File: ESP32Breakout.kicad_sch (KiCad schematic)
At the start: 7 parts, among them U1 ESP32-S3

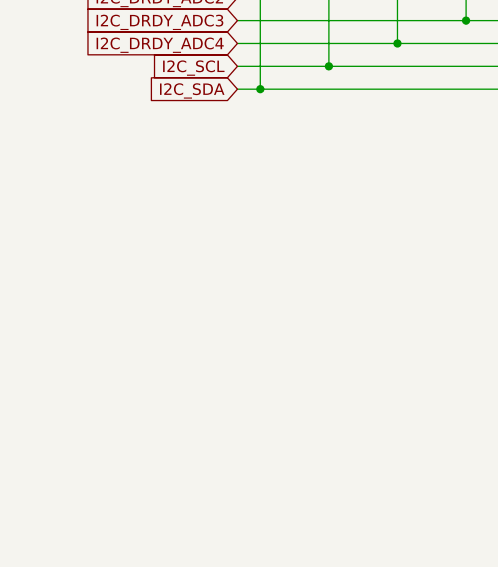
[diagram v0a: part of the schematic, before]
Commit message: Add valve control
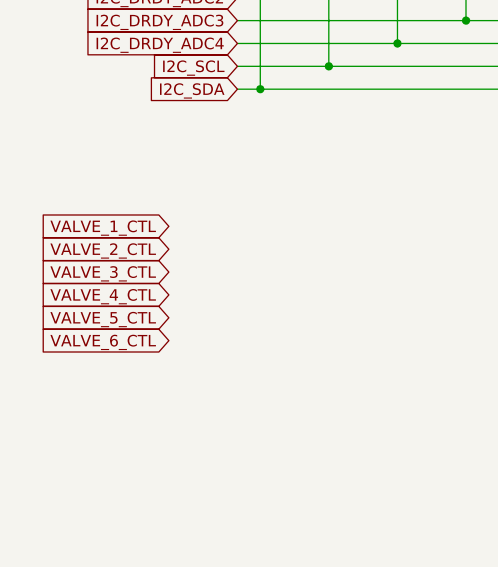
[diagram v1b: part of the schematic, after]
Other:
- company: (none) -> Queen's Rocket Engineering Team
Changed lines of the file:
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@@
 	(generator_version "9.0")
 	(paper "A4")
+	(title_block
+		(rev "0.1.0")
+		(company "Queen's Rocket Engineering Team")
+	)
 	(junction
 		(at 66.04 63.5)
@@
 		)
 	)
+	(global_label "VALVE_6_CTL"
+		(shape input)
+		(at 48.26 93.98 180)
+		(fields_autoplaced yes)
+		(effects
+			(font
+				(size 1.27 1.27)
+			)
+			(justify right)
+		)
+		(property "Intersheetrefs" "${INTERSHEET_REFS}"
+			(at 33.4215 93.98 0)
+			(effects
+				(font
+					(size 1.27 1.27)
+				)
+				(justify right)
+				(hide yes)
+			)
+		)
+	)
+	(global_label "VALVE_1_CTL"
+		(shape input)
+		(at 48.26 81.28 180)
+		(fields_autoplaced yes)
+		(effects
+			(font
+				(size 1.27 1.27)
+			)
+			(justify right)
+		)
+		(property "Intersheetrefs" "${INTERSHEET_REFS}"
+			(at 33.4215 81.28 0)
+			(effects
+				(font
+					(size 1.27 1.27)
+				)
+				(justify right)
+				(hide yes)
+			)
+		)
+	)
 	(global_label "I2C_SCL"
 		(shape input)
@@
 		)
 	)
+	(global_label "VALVE_5_CTL"
+		(shape input)
+		(at 48.26 91.44 180)
+		(fields_autoplaced yes)
+		(effects
+			(font
+				(size 1.27 1.27)
+			)
+			(justify right)
+		)
+		(property "Intersheetrefs" "${INTERSHEET_REFS}"
+			(at 33.4215 91.44 0)
+			(effects
+				(font
+					(size 1.27 1.27)
+				)
+				(justify right)
+				(hide yes)
+			)
+		)
+	)
+	(global_label "VALVE_4_CTL"
+		(shape input)
+		(at 48.26 88.9 180)
+		(fields_autoplaced yes)
+		(effects
+			(font
+				(size 1.27 1.27)
+			)
+			(justify right)
+		)
+		(property "Intersheetrefs" "${INTERSHEET_REFS}"
+			(at 33.4215 88.9 0)
+			(effects
+				(font
+					(size 1.27 1.27)
+				)
+				(justify right)
+				(hide yes)
+			)
+		)
+	)
 	(global_label "I2C_DRDY_ADC1"
 		(shape input)
@@
 		)
 	)
+	(global_label "VALVE_3_CTL"
+		(shape input)
+		(at 48.26 86.36 180)
+		(fields_autoplaced yes)
+		(effects
+			(font
+				(size 1.27 1.27)
+			)
+			(justify right)
+		)
+		(property "Intersheetrefs" "${INTERSHEET_REFS}"
+			(at 33.4215 86.36 0)
+			(effects
+				(font
+					(size 1.27 1.27)
+				)
+				(justify right)
+				(hide yes)
+			)
+		)
+	)
 	(global_label "I2C_DRDY_ADC2"
 		(shape input)
@@
 			(effects
 				(font
+					(size 1.27 1.27)
+				)
+				(justify right)
+				(hide yes)
+			)
+		)
+	)
+	(global_label "VALVE_2_CTL"
+		(shape input)
+		(at 48.26 83.82 180)
+		(fields_autoplaced yes)
+		(effects
+			(font
+				(size 1.27 1.27)
+			)
+			(justify right)
+		)
+		(property "Intersheetrefs" "${INTERSHEET_REFS}"
+			(at 33.4215 83.82 0)
+			(effects
+				(font
